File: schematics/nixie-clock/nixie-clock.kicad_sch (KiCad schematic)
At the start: 49 parts, among them J1 Barrel_Jack_Switch, J2 Conn_02x03_Odd_Even, J3 Screw_Terminal_01x02, J4 Screw_Terminal_01x02, Q1 MJE13007, Q2 MJE13007, SW1 SW_Push, SW2 SW_Push, SW3 SW_Push, U1 LM317_TO-220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

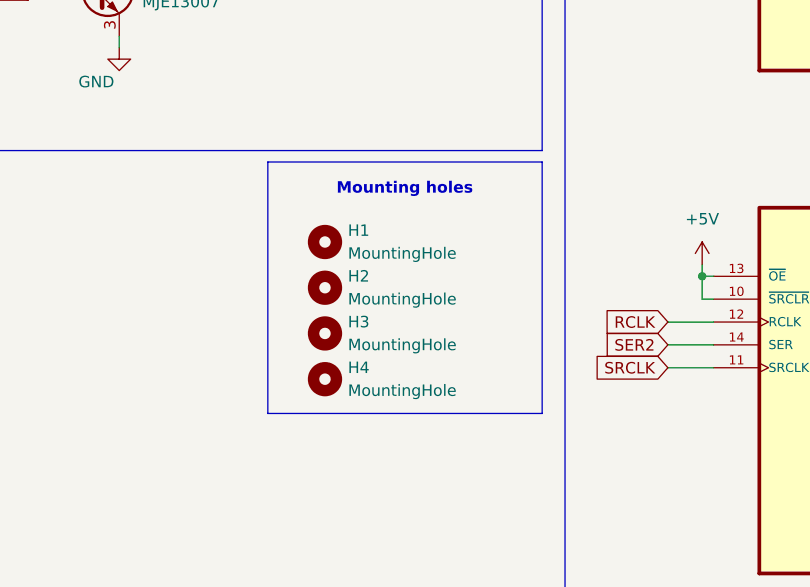
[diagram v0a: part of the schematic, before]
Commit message: schematics: asigned footprints, started working on PCB, modified in-1 footprint
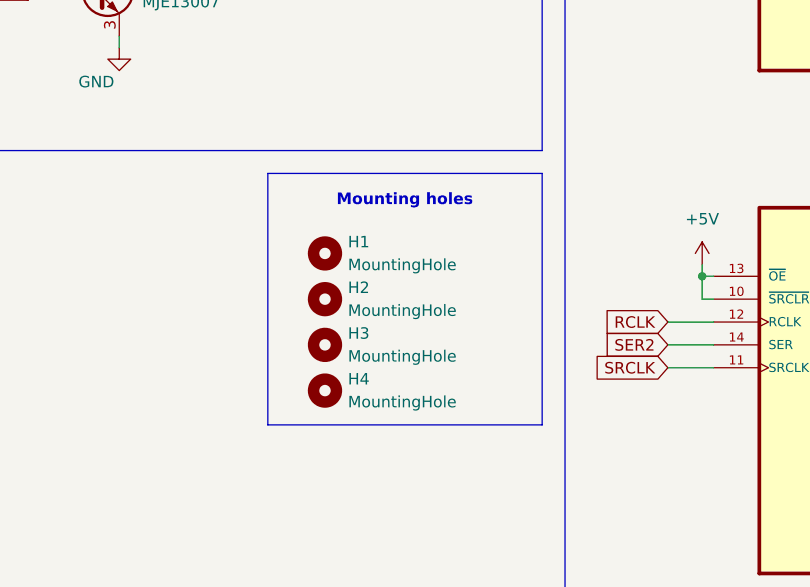
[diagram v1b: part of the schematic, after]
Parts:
- N1, N2, N3, N4: footprint nixies-us:nixies-us-IN-1 -> IN1:IN-1
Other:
- moved on the sheet: H1, H2, H3, H4
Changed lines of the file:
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@@
     (stroke (width 0) (type default) (color 0 0 0 0))
   )
-  (polyline (pts (xy 289.56 203.2) (xy 289.56 231.14))
+  (polyline (pts (xy 289.56 204.47) (xy 289.56 232.41))
     (stroke (width 0) (type default) (color 0 0 0 0))
   )
@@
     (stroke (width 0) (type default) (color 0 0 0 0))
   )
-  (polyline (pts (xy 320.04 203.2) (xy 289.56 203.2))
+  (polyline (pts (xy 320.04 204.47) (xy 289.56 204.47))
     (stroke (width 0) (type default) (color 0 0 0 0))
   )
@@
     (stroke (width 0) (type default) (color 0 0 0 0))
   )
-  (polyline (pts (xy 289.56 231.14) (xy 320.04 231.14))
+  (polyline (pts (xy 289.56 232.41) (xy 320.04 232.41))
     (stroke (width 0) (type default) (color 0 0 0 0))
   )
@@
     (stroke (width 0) (type default) (color 0 0 0 0))
   )
-  (polyline (pts (xy 320.04 203.2) (xy 320.04 231.14))
+  (polyline (pts (xy 320.04 204.47) (xy 320.04 232.41))
     (stroke (width 0) (type default) (color 0 0 0 0))
   )
@@
     (effects (font (size 1.27 1.27) bold) (justify left bottom))
   )
-  (text "Mounting holes" (at 297.18 207.01 0)
+  (text "Mounting holes" (at 297.18 208.28 0)
     (effects (font (size 1.27 1.27) (thickness 0.254) bold) (justify left bottom))
   )
@@
     (pin "9")
   )
-  (symbol (lib_id "Mechanical:MountingHole") (at 295.91 227.33 0) (unit 1)
+  (symbol (lib_id "Mechanical:MountingHole") (at 295.91 228.6 0) (unit 1)
     (in_bom yes) (on_board yes) (fields_autoplaced)
-    (property "Reference" "H4" (id 0) (at 298.45 226.0599 0)
+    (property "Reference" "H4" (id 0) (at 298.45 227.3299 0)
       (effects (font (size 1.27 1.27)) (justify left))
     )
-    (property "Value" "MountingHole" (id 1) (at 298.45 228.5999 0)
+    (property "Value" "MountingHole" (id 1) (at 298.45 229.8699 0)
       (effects (font (size 1.27 1.27)) (justify left))
     )
-    (property "Footprint" "MountingHole:MountingHole_3mm" (id 2) (at 295.91 227.33 0)
+    (property "Footprint" "MountingHole:MountingHole_3mm" (id 2) (at 295.91 228.6 0)
       (effects (font (size 1.27 1.27)) hide)
     )
-    (property "Datasheet" "~" (id 3) (at 295.91 227.33 0)
+    (property "Datasheet" "~" (id 3) (at 295.91 228.6 0)
       (effects (font (size 1.27 1.27)) hide)
     )
@@
       (effects (font (size 1.143 1.143)) (justify left bottom) hide)
     )
-    (property "Footprint" "nixies-us:nixies-us-IN-1" (id 2) (at 264.922 105.41 0)
+    (property "Footprint" "IN1:IN-1" (id 2) (at 264.922 105.41 0)
       (effects (font (size 0.508 0.508)) hide)
     )
@@
       (effects (font (size 1.143 1.143)) (justify left bottom) hide)
     )
-    (property "Footprint" "nixies-us:nixies-us-IN-1" (id 2) (at 376.682 106.68 0)
+    (property "Footprint" "IN1:IN-1" (id 2) (at 376.682 106.68 0)
       (effects (font (size 0.508 0.508)) hide)
     )
@@
     (pin "A")
   )
-  (symbol (lib_id "Mechanical:MountingHole") (at 295.91 217.17 0) (unit 1)
+  (symbol (lib_id "Mechanical:MountingHole") (at 295.91 218.44 0) (unit 1)
     (in_bom yes) (on_board yes) (fields_autoplaced)
-    (property "Reference" "H2" (id 0) (at 298.45 215.8999 0)
+    (property "Reference" "H2" (id 0) (at 298.45 217.1699 0)
       (effects (font (size 1.27 1.27)) (justify left))
     )
-    (property "Value" "MountingHole" (id 1) (at 298.45 218.4399 0)
+    (property "Value" "MountingHole" (id 1) (at 298.45 219.7099 0)
       (effects (font (size 1.27 1.27)) (justify left))
     )
-    (property "Footprint" "MountingHole:MountingHole_3mm" (id 2) (at 295.91 217.17 0)
+    (property "Footprint" "MountingHole:MountingHole_3mm" (id 2) (at 295.91 218.44 0)
       (effects (font (size 1.27 1.27)) hide)
     )
-    (property "Datasheet" "~" (id 3) (at 295.91 217.17 0)
+    (property "Datasheet" "~" (id 3) (at 295.91 218.44 0)
       (effects (font (size 1.27 1.27)) hide)
     )
@@
       (effects (font (size 1.143 1.143)) (justify left bottom) hide)
     )
-    (property "Footprint" "nixies-us:nixies-us-IN-1" (id 2) (at 264.922 48.26 0)
+    (property "Footprint" "IN1:IN-1" (id 2) (at 264.922 48.26 0)
       (effects (font (size 0.508 0.508)) hide)
     )
@@
       (effects (font (size 1.143 1.143)) (justify left bottom) hide)
     )
-    (property "Footprint" "nixies-us:nixies-us-IN-1" (id 2) (at 376.682 49.53 0)
+    (property "Footprint" "IN1:IN-1" (id 2) (at 376.682 49.53 0)
       (effects (font (size 0.508 0.508)) hide)
     )
@@
     (pin "1")
   )
-  (symbol (lib_id "Mechanical:MountingHole") (at 295.91 222.25 0) (unit 1)
+  (symbol (lib_id "Mechanical:MountingHole") (at 295.91 223.52 0) (unit 1)
     (in_bom yes) (on_board yes) (fields_autoplaced)
-    (property "Reference" "H3" (id 0) (at 298.45 220.9799 0)
+    (property "Reference" "H3" (id 0) (at 298.45 222.2499 0)
       (effects (font (size 1.27 1.27)) (justify left))
     )
-    (property "Value" "MountingHole" (id 1) (at 298.45 223.5199 0)
+    (property "Value" "MountingHole" (id 1) (at 298.45 224.7899 0)
       (effects (font (size 1.27 1.27)) (justify left))
     )
-    (property "Footprint" "MountingHole:MountingHole_3mm" (id 2) (at 295.91 222.25 0)
+    (property "Footprint" "MountingHole:MountingHole_3mm" (id 2) (at 295.91 223.52 0)
       (effects (font (size 1.27 1.27)) hide)
     )
-    (property "Datasheet" "~" (id 3) (at 295.91 222.25 0)
+    (property "Datasheet" "~" (id 3) (at 295.91 223.52 0)
       (effects (font (size 1.27 1.27)) hide)
     )
@@
     (pin "2")
   )
-  (symbol (lib_id "Mechanical:MountingHole") (at 295.91 212.09 0) (unit 1)
+  (symbol (lib_id "Mechanical:MountingHole") (at 295.91 213.36 0) (unit 1)
     (in_bom yes) (on_board yes) (fields_autoplaced)
-    (property "Reference" "H1" (id 0) (at 298.45 210.8199 0)
+    (property "Reference" "H1" (id 0) (at 298.45 212.0899 0)
       (effects (font (size 1.27 1.27)) (justify left))
     )
-    (property "Value" "MountingHole" (id 1) (at 298.45 213.3599 0)
+    (property "Value" "MountingHole" (id 1) (at 298.45 214.6299 0)
       (effects (font (size 1.27 1.27)) (justify left))
     )
-    (property "Footprint" "MountingHole:MountingHole_3mm" (id 2) (at 295.91 212.09 0)
+    (property "Footprint" "MountingHole:MountingHole_3mm" (id 2) (at 295.91 213.36 0)
       (effects (font (size 1.27 1.27)) hide)
     )
-    (property "Datasheet" "~" (id 3) (at 295.91 212.09 0)
+    (property "Datasheet" "~" (id 3) (at 295.91 213.36 0)
       (effects (font (size 1.27 1.27)) hide)
     )
@@
     )
     (path "/819cd935-2cda-47a0-b6b4-1364c82c84b7"
-      (reference "N1") (unit 1) (value "IN-1") (footprint "nixies-us:nixies-us-IN-1")
+      (reference "N1") (unit 1) (value "IN-1") (footprint "IN1:IN-1")
     )
     (path "/2f78acd8-feba-4edb-a624-ff5c6af6307b"
-      (reference "N2") (unit 1) (value "IN-1") (footprint "nixies-us:nixies-us-IN-1")
+      (reference "N2") (unit 1) (value "IN-1") (footprint "IN1:IN-1")
     )
     (path "/aa35d094-0eb9-45cb-bb2e-b75cdebf8981"
-      (reference "N3") (unit 1) (value "IN-1") (footprint "nixies-us:nixies-us-IN-1")
+      (reference "N3") (unit 1) (value "IN-1") (footprint "IN1:IN-1")
     )
     (path "/61e30a05-e9e6-460b-9a1c-8c82888c9101"
-      (reference "N4") (unit 1) (value "IN-1") (footprint "nixies-us:nixies-us-IN-1")
+      (reference "N4") (unit 1) (value "IN-1") (footprint "IN1:IN-1")
     )
     (path "/e74e1929-c6c3-4397-ad9d-3dc08d146b81"

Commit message: schematic correction: added anode resistors for nixie tubes
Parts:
- added R11, R12, R13, R14, R15, R16, R17, R18: 33k, symbol Device:R
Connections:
- net HIGH VOLTAGE: now also R11.2, R12.2, R13.2, R14.2, R15.2, R16.2, R17.2, R18.2; no longer N1.A, N2.A, N3.A, N4.A
- new net: N2.A, R13.1, R14.1
- new net: N1.A, R11.1, R12.1
- new net: N4.A, R17.1, R18.1
- new net: N3.A, R15.1, R16.1
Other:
- moved on the sheet: N1, N3, N4, U5, U7, U8

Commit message: annotated some more components idk
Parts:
- added H5, H6, H7, H8: MountingHole, MountingHole:MountingHole_3mm, symbol Mechanical:MountingHole
- added J5, J9: Screw_Terminal_01x03, symbol Connector:Screw_Terminal_01x03
- added J6, J7: Conn_01x03, symbol Connector_Generic:Conn_01x03
- added J8: Conn_01x04, symbol Connector_Generic:Conn_01x04
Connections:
- net +5V: now also J5.2 (Pin_2), J8.1 (Pin_1)
- net GND: now also J5.3 (Pin_3), J8.4 (Pin_4)
- net HIGH VOLTAGE: now also J9.3 (Pin_3); no longer J4.2 (Pin_2)
- net RCLK: now also J7.2 (Pin_2); no longer U2.25 (PC2)
- net SER1: now also J7.3 (Pin_3); no longer U2.23 (PC0)
- net SRCLK: now also J7.1 (Pin_1); no longer U2.24 (PC1)
- net RTC_SCL renamed SCL
- net SCL: now also J8.3 (Pin_3)
- net RTC_SDA renamed SDA
- net SDA: now also J8.2 (Pin_2)
- new net +5VA: J9.2 (Pin_2)
- new net BOOSTER OUT: J4.2 (Pin_2), J5.1 (Pin_1)
- new net GNDA: J9.1 (Pin_1)
- new net RCLK_CON: J6.2 (Pin_2), U2.25 (PC2)
- new net SER1_CON: J6.1 (Pin_1), U2.23 (PC0)
- new net SRCLK_CON: J6.3 (Pin_3), U2.24 (PC1)
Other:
- moved on the sheet: H1, H2, H3, H4

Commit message: schematic: added inter-panel connection
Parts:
- removed J6, J7: Conn_01x03, symbol Connector_Generic:Conn_01x03
- added J? (x2): Conn_01x07, symbol Connector_Generic:Conn_01x07
- J5, J9: footprint (none) -> TerminalBlock_Phoenix:TerminalBlock_Phoenix_MKDS-1,5-3_1x03_P5.00mm_Horizontal
- J8: footprint (none) -> Connector_PinHeader_2.54mm:PinHeader_1x03_P2.54mm_Horizontal
- R11, R12, R13, R14, R15, R16, R17, R18: footprint (none) -> Resistor_THT:R_Axial_DIN0309_L9.0mm_D3.2mm_P12.70mm_Horizontal
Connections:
- net +5V: now also J?.1 (Pin_1)
- net +5VA: now also J?.7 (Pin_7)
- net BULB1: now also J?.3 (Pin_3); no longer U2.2 (PD0)
- net BULB2: now also J?.2 (Pin_2); no longer U2.3 (PD1)
- net GND: now also J?.7 (Pin_7)
- net GNDA: now also J?.1 (Pin_1)
- net RCLK: now also J?.5 (Pin_5)
- net RCLK_CON: now also J?.3 (Pin_3)
- net SER1: now also J?.6 (Pin_6)
- net SER1_CON: now also J?.2 (Pin_2)
- net SRCLK: now also J?.4 (Pin_4)
- net SRCLK_CON: now also J?.4 (Pin_4)
- new net BULB1_CON: J?.5 (Pin_5), U2.2 (PD0)
- new net BULB2_CON: J?.6 (Pin_6), U2.3 (PD1)
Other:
- note added: "Front panel connections"
- note added: "I²C Header"
- moved on the sheet: J8

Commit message: schematic: corrected connectors, separated front and back panel power pins
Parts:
- removed J5, J9: Screw_Terminal_01x03, TerminalBlock_Phoenix:TerminalBlock_Phoenix_MKDS-1,5-3_1x03_P5.00mm_Horizontal, symbol Connector:Screw_Terminal_01x03
- J4: footprint TerminalBlock_Phoenix:TerminalBlock_Phoenix_MKDS-1,5-2_1x02_P5.00mm_Horizontal -> (none)
- gave numbers to parts that had none: 2
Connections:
- net BOOSTER OUT is gone; now on net HIGH VOLTAGE: J4.2 (Pin_2)
- net +5V: no longer U3.10 (~{SRCLR}), U3.13 (~{OE}), U3.16 (VCC), U4.10 (~{SRCLR}), U4.13 (~{OE}), U4.16 (VCC), U5.5 (VCC), U6.5 (VCC), U7.5 (VCC), U8.5 (VCC)
- net +5VA: now also U3.10 (~{SRCLR}), U3.13 (~{OE}), U3.16 (VCC), U4.10 (~{SRCLR}), U4.13 (~{OE}), U4.16 (VCC), U5.5 (VCC), U6.5 (VCC), U7.5 (VCC), U8.5 (VCC)
- net GND: no longer J4.1 (Pin_1), Q1.3 (E), Q2.3 (E), U3.8 (GND), U4.8 (GND), U5.12 (GND), U6.12 (GND), U7.12 (GND), U8.12 (GND)
- net GNDA: now also Q1.3 (E), Q2.3 (E), U3.8 (GND), U4.8 (GND), U5.12 (GND), U6.12 (GND), U7.12 (GND), U8.12 (GND)
- no-connect marks 10 -> 11
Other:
- note added: "Back panel side"
- note added: "Front panel side"

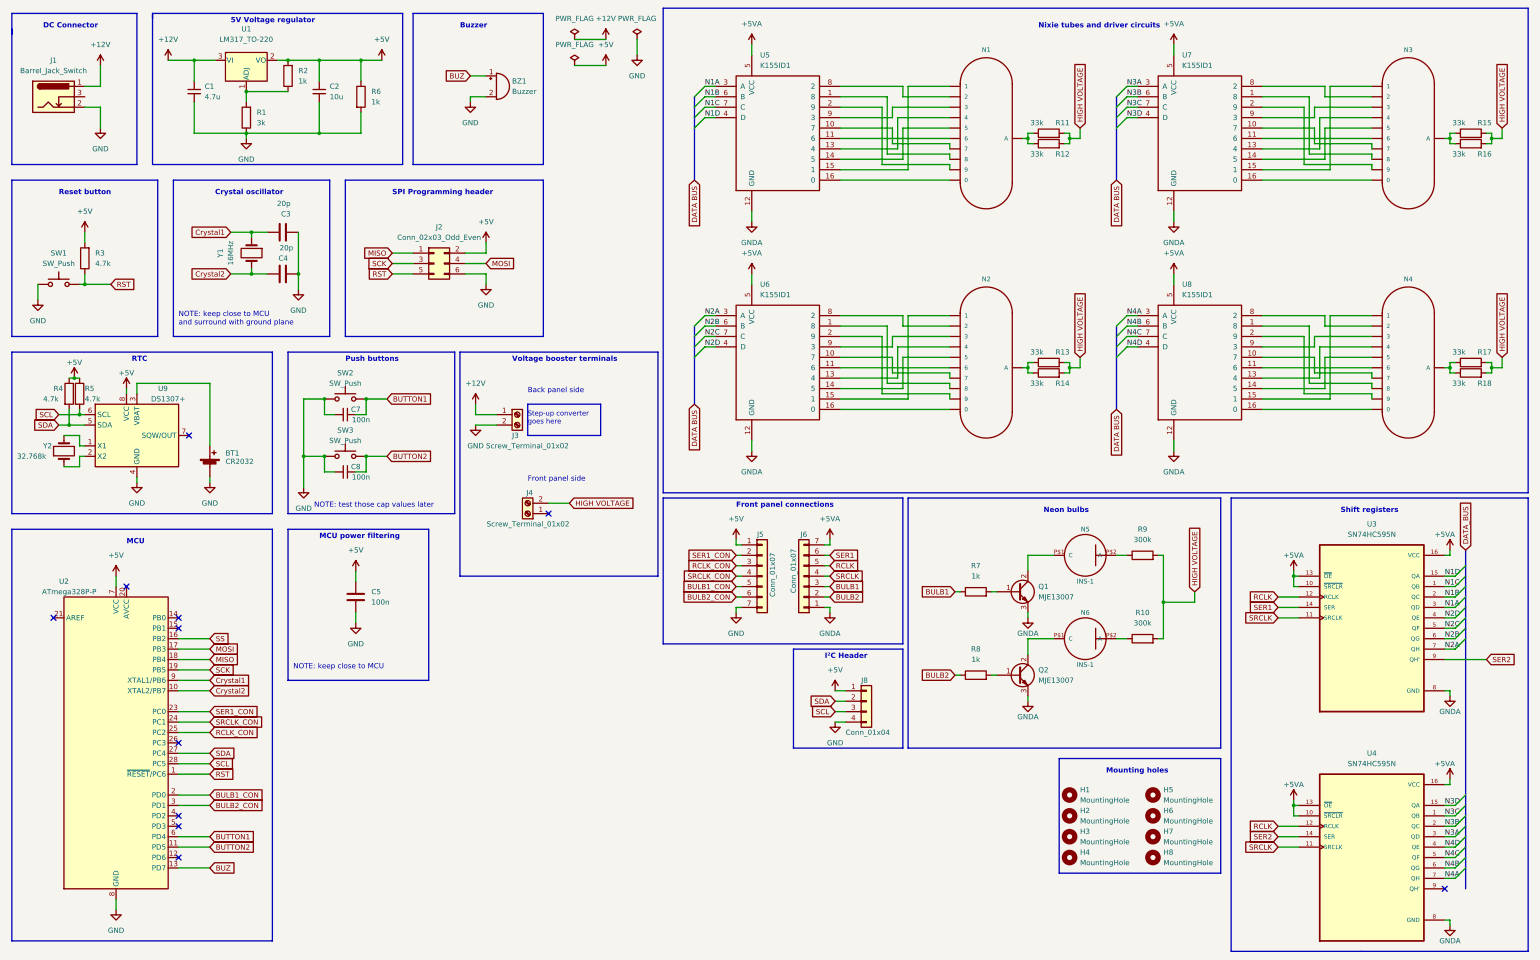
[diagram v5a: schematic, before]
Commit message: pcb: placed elements on main board, added mounting holes
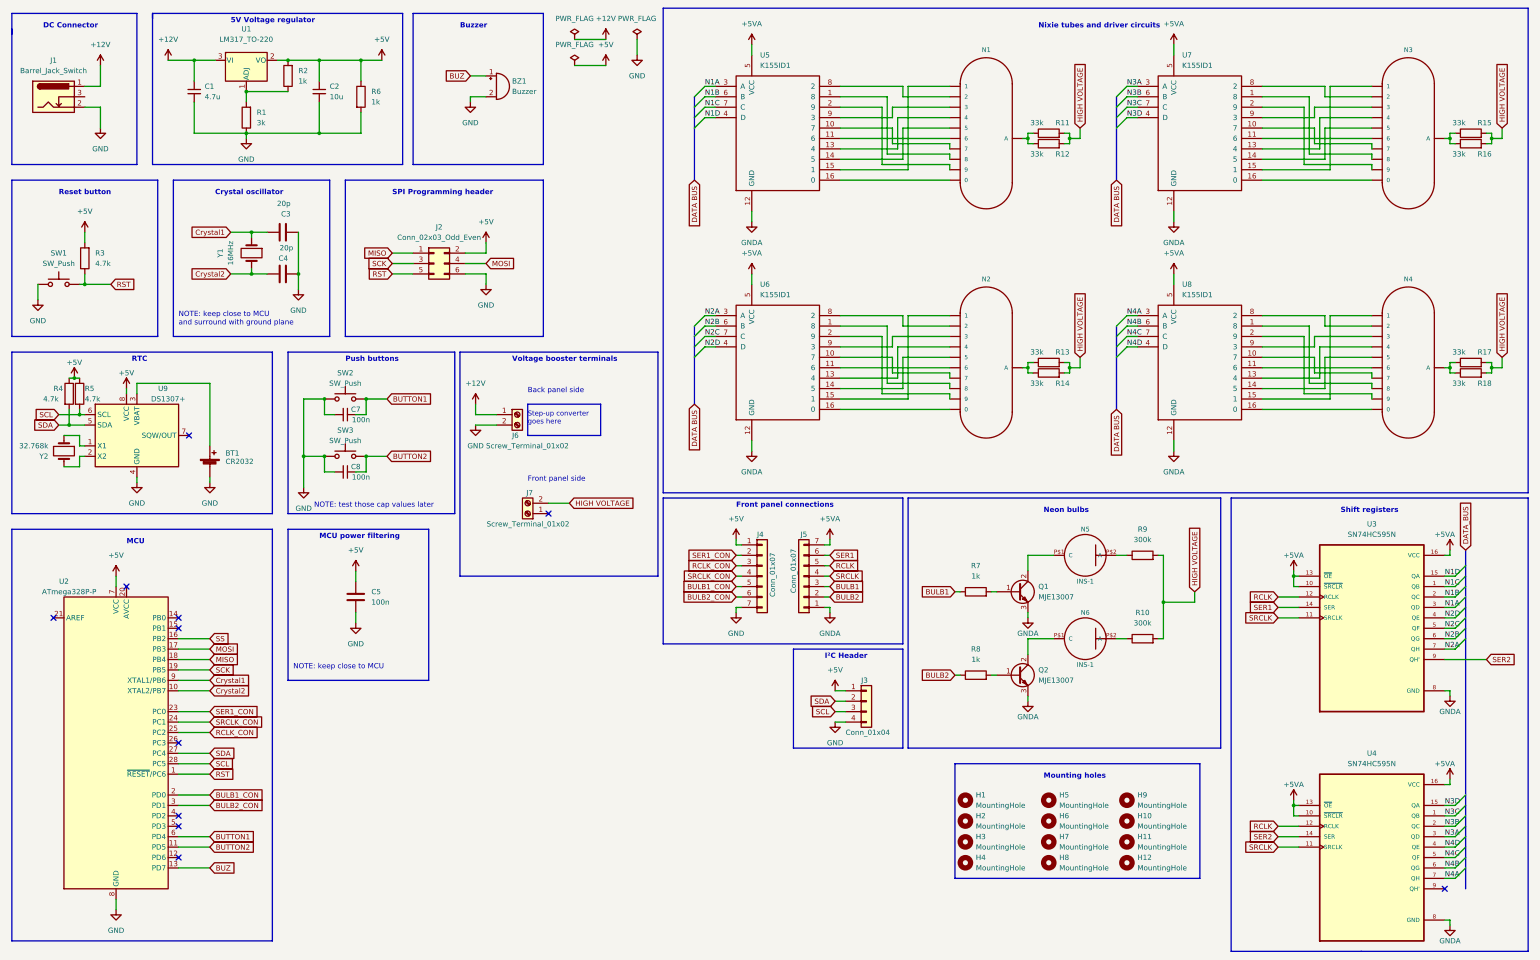
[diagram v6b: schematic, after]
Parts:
- added H10, H11, H12, H9: MountingHole, MountingHole:MountingHole_3mm, symbol Mechanical:MountingHole
- J3: renamed from J8; footprint Connector_PinHeader_2.54mm:PinHeader_1x03_P2.54mm_Horizontal -> Connector_PinHeader_2.54mm:PinHeader_1x04_P2.54mm_Vertical
- J4: renamed from J5; footprint (none) -> Connector_PinHeader_2.54mm:PinHeader_1x07_P2.54mm_Horizontal
- J5: renamed from J6; footprint (none) -> Connector_PinHeader_2.54mm:PinHeader_1x07_P2.54mm_Horizontal
- J7: renamed from J4; footprint (none) -> TerminalBlock_Phoenix:TerminalBlock_Phoenix_MKDS-1,5-2_1x02_P5.00mm_Horizontal
- SW2, SW3: footprint Button_Switch_Keyboard:SW_Cherry_MX_1.00u_PCB -> Button_Switch_THT:SW_PUSH_6mm_H13mm
- renumbered J3 to J6
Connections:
- net at U9.1 (X1): now also Y2.1; no longer Y2.2
- net at U9.2 (X2): now also Y2.2; no longer Y2.1
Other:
- moved on the sheet: H1, H2, H3, H4, H5, H6, H7, H8, Y2
